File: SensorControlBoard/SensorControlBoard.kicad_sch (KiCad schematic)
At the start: 0 parts

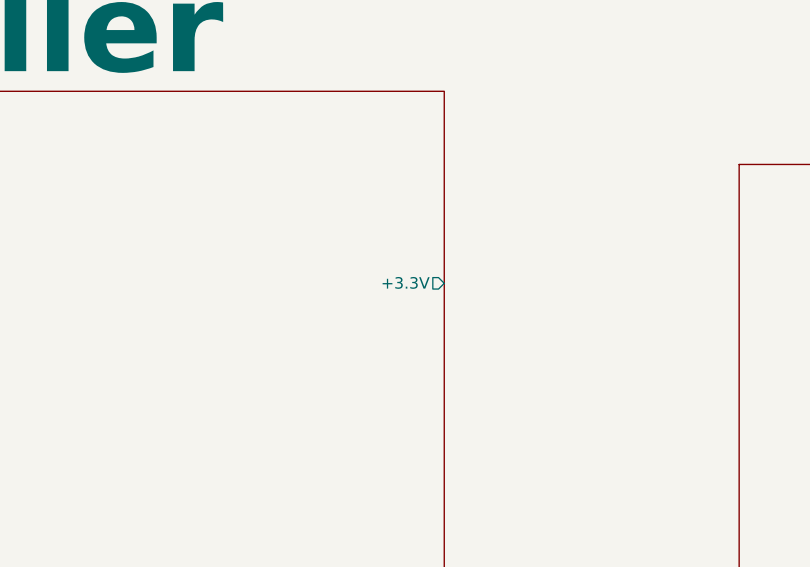
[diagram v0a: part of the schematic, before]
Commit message: Implemented ICM-42670-P 6 axis gyroscope/accelerometer
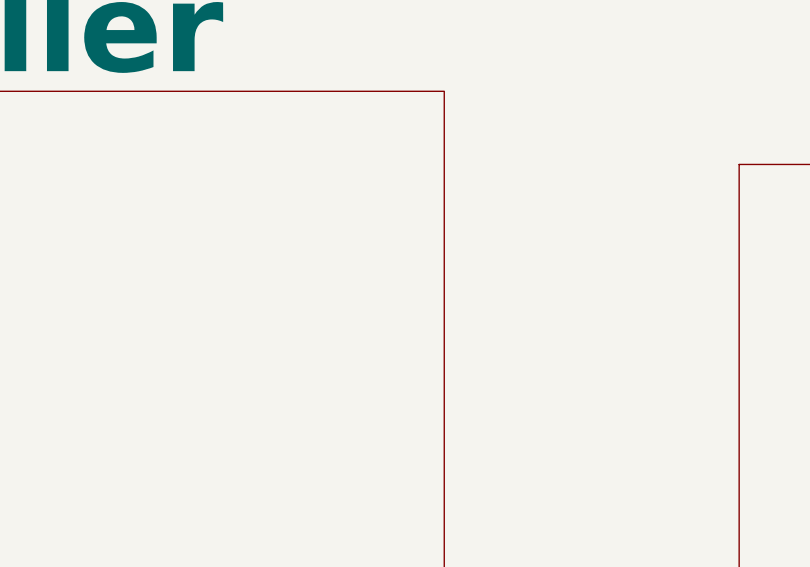
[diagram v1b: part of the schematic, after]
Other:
- sheet uController ports: added none; removed +3.3V
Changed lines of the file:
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@@
       (effects (font (size 5 5)) (justify left top))
-    )
-    (pin "+3.3V" output (at 157.226 113.284 0)
-      (effects (font (size 1.27 1.27)) (justify right))
     )
     (instances

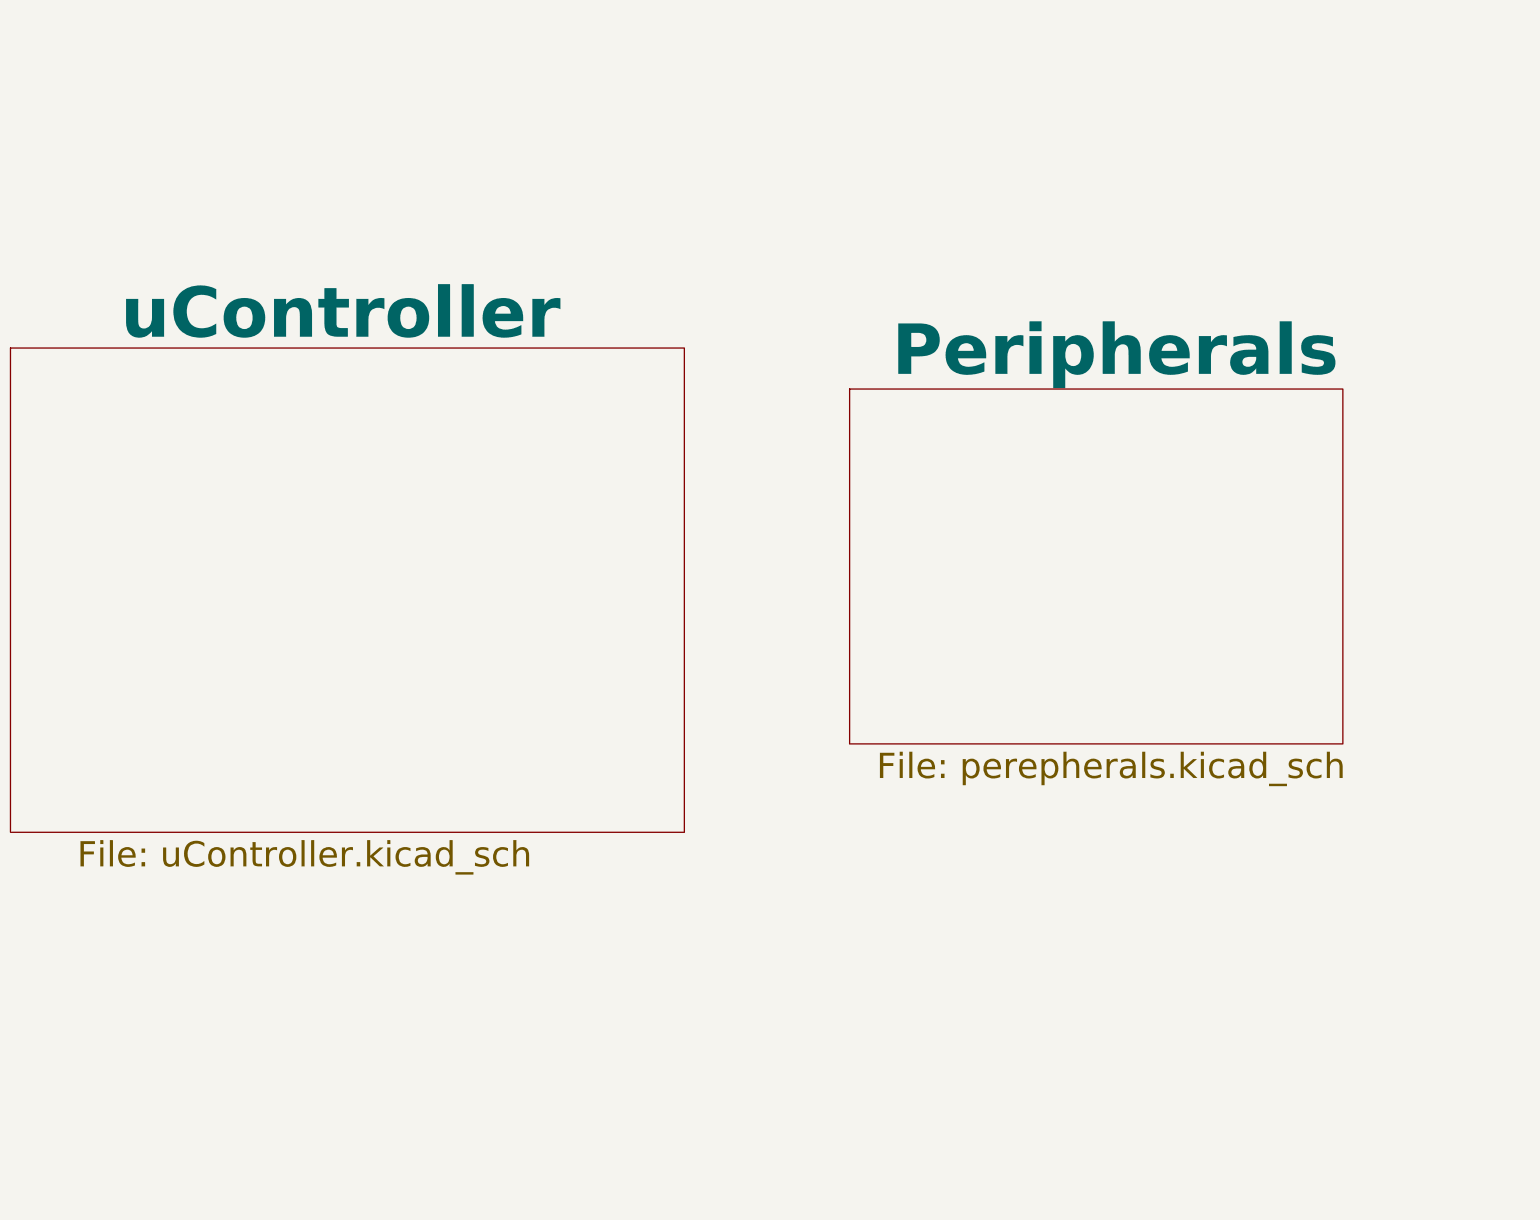
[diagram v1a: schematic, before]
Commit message: Added more schematic documentation to prepare for hardware layout
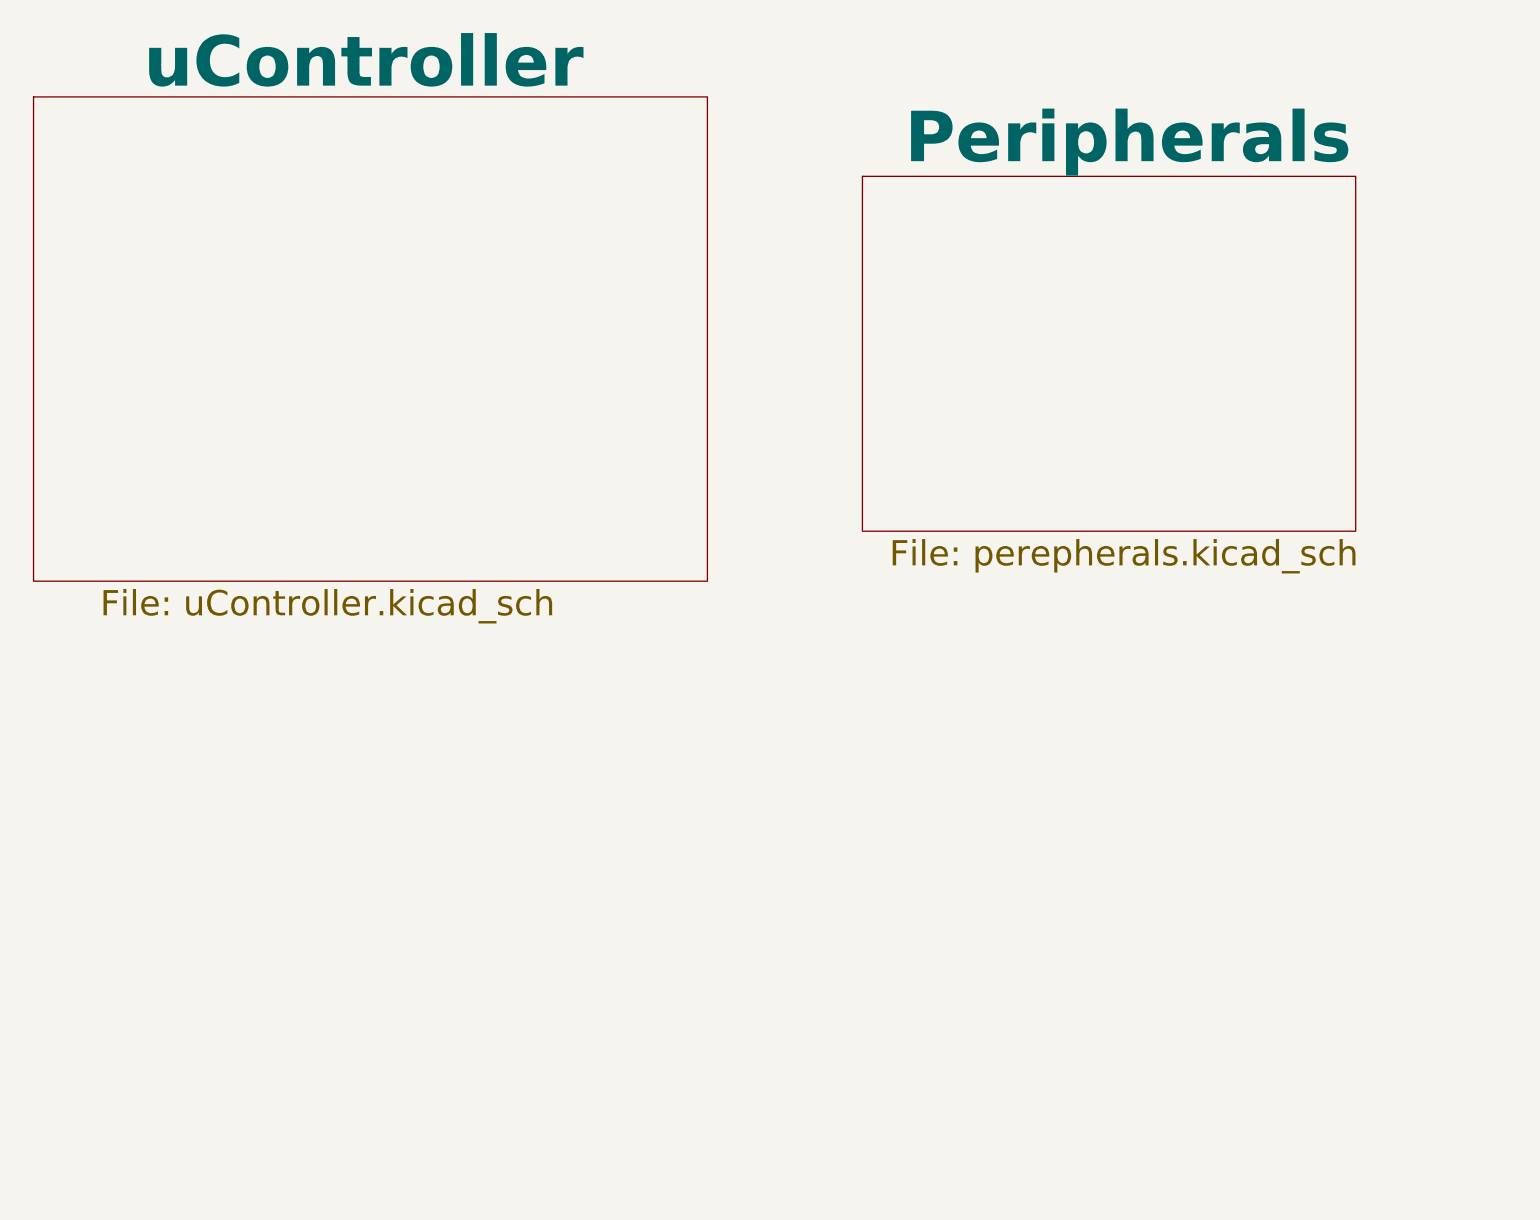
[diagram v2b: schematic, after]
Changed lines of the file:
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@@
     (company "EEC")
   )
-  (sheet (at 189.992 100.076) (size 97.79 70.358)
+  (sheet (at 192.532 57.912) (size 97.79 70.358)
     (stroke (width 0.1524) (type solid))
     (fill (color 0 0 0 0.0000))
-    (property "Sheetname" "Peripherals" (at 198.374 98.298 0)
+    (property "Sheetname" "Peripherals" (at 200.914 56.134 0)
       (effects (font (size 10 10) bold) (justify left bottom))
     )
-    (property "Sheetfile" "perepherals.kicad_sch" (at 195.326 171.958 0)
+    (property "Sheetfile" "perepherals.kicad_sch" (at 197.866 129.794 0)
       (effects (font (size 5 5)) (justify left top))
     )
@@
     )
   )
-  (sheet (at 23.622 91.948) (size 133.604 96.012)
+  (sheet (at 28.194 42.164) (size 133.604 96.012)
     (stroke (width 0.1524) (type solid))
     (fill (color 0 0 0 0.0000))
-    (property "Sheetname" "uController" (at 45.466 90.932 0)
+    (property "Sheetname" "uController" (at 50.038 41.148 0)
       (effects (font (size 10 10) bold) (justify left bottom))
     )
-    (property "Sheetfile" "uController.kicad_sch" (at 36.83 189.484 0)
+    (property "Sheetfile" "uController.kicad_sch" (at 41.402 139.7 0)
       (effects (font (size 5 5)) (justify left top))
     )

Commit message: Initial Routing finished
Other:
- added sheet Misc (Misc.kicad_sch)
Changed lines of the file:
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@@
+    )
+  )
+  (sheet (at 133.096 166.37) (size 82.804 87.63)
+    (stroke (width 0.1524) (type solid))
+    (fill (color 0 0 0 0.0000))
+    (property "Sheetname" "Misc" (at 156.21 165.608 0)
+      (effects (font (size 10 10) bold) (justify left bottom))
+    )
+    (property "Sheetfile" "Misc.kicad_sch" (at 133.096 254.5846 0)
+      (effects (font (size 5 5)) (justify left top))
+    )
+    (instances
+      (project "SensorControlBoard"
+        (path "/8c0c4014-aa51-4bf6-8434-aa4d122163d4" (page "4"))
+      )
     )
   )
